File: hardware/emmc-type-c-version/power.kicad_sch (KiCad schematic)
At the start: 25 parts, among them SW301 RESET SW, U301 SPX3819M5-L

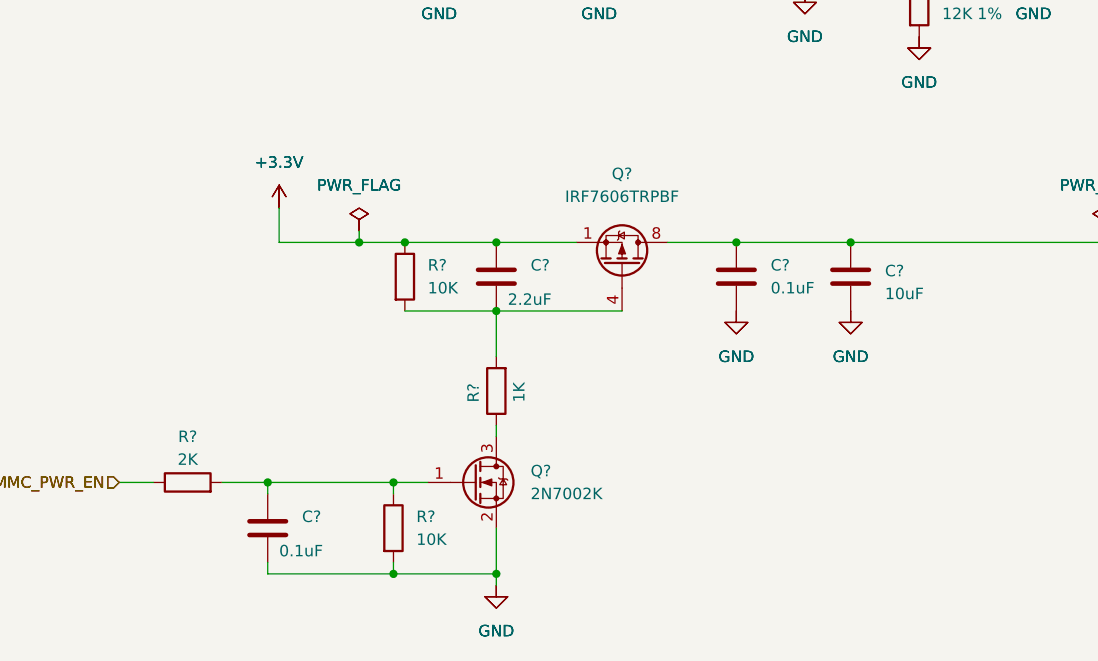
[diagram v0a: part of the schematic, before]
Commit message: Corrected part number in the BOM
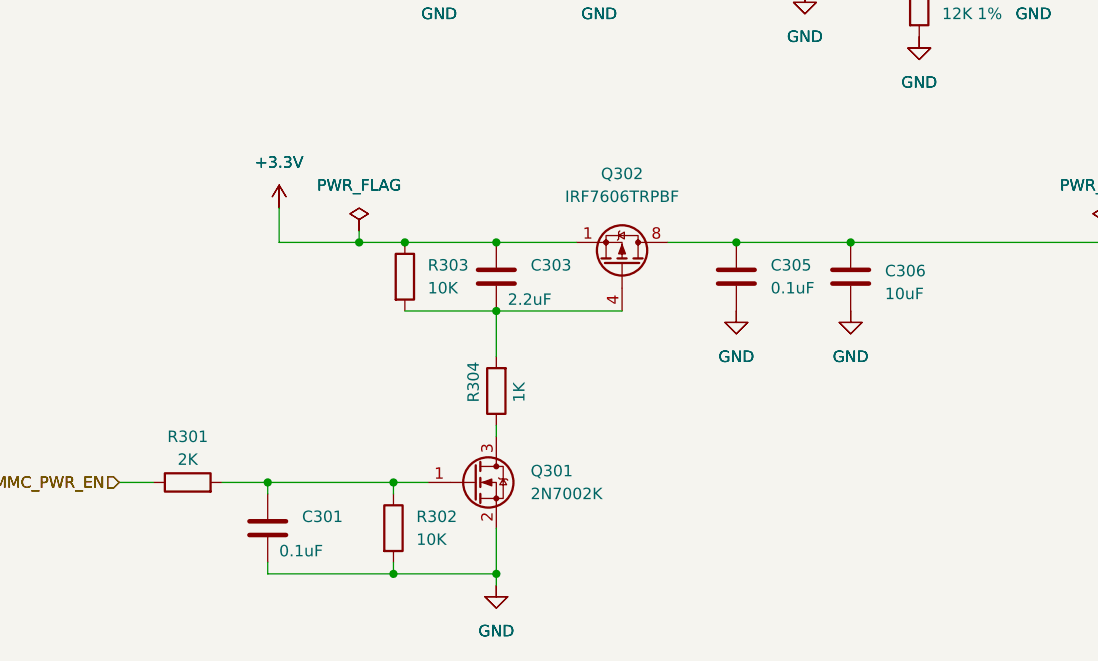
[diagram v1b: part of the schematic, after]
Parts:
- C304, C308: digikey 311-3494-1-ND -> 311-1355-1-ND; storeURL https://www.digikey.com/en/products/detail/yageo/CC0603MRX5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 -> https://www.digikey.com/en/products/detail/yageo/CC0805ZKY5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
- C306: renamed from C?; digikey 311-3494-1-ND -> 311-1355-1-ND; storeURL https://www.digikey.com/en/products/detail/yageo/CC0603MRX5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 -> https://www.digikey.com/en/products/detail/yageo/CC0805ZKY5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
- FB301: footprint tbctl:L_0603_1608Metric_Pad1.05x0.95mm_HandSolder -> Inductor_SMD:L_0603_1608Metric_Pad1.05x0.95mm_HandSolder; digikey 240-2399-1-ND -> 490-1014-1-ND; storeURL https://www.digikey.com/en/products/detail/laird-signal-int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 -> https://www.digikey.com/en/products/detail/murata-electroni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
- R301: renamed from R?; footprint tbctl:R_0805_2012Metric_Pad1.20x1.40mm_HandSolder -> Resistor_SMD:R_0805_2012Metric_Pad1.20x1.40mm_HandSolder; digikey 311-2.0KGRCT-ND -> 311-2.0KARCT-ND; storeURL https://www.digikey.com/en/products/detail/yageo/RC0603JR-0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 -> https://www.digikey.com/en/products/detail/yageo/RC0805JR-0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
- R302, R303: renamed from R?; footprint tbctl:R_0805_2012Metric_Pad1.20x1.40mm_HandSolder -> Resistor_SMD:R_0805_2012Metric_Pad1.20x1.40mm_HandSolder; digikey 13-RC0603JR-1010KLCT-ND -> 311-10KARCT-ND; storeURL https://www.digikey.com/en/products/detail/yageo/RC0603JR-1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 -> https://www.digikey.com/en/products/detail/yageo/RC0805JR-0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
- R304: renamed from R?; footprint tbctl:R_0805_2012Metric_Pad1.20x1.40mm_HandSolder -> Resistor_SMD:R_0805_2012Metric_Pad1.20x1.40mm_HandSolder; digikey 13-RC0603JR-101KLCT-ND -> 311-1.0KARCT-ND; storeURL https://www.digikey.com/en/products/detail/yageo/RC0603JR-1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 -> https://www.digikey.com/en/products/detail/yageo/RC0805JR-0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
- R305: footprint tbctl:R_0805_2012Metric_Pad1.20x1.40mm_HandSolder -> Resistor_SMD:R_0805_2012Metric_Pad1.20x1.40mm_HandSolder; digikey 13-RC0603FR-1320KLCT-ND -> 311-20.0KCRCT-ND; storeURL https://www.digikey.com/en/products/detail/yageo/RC0603FR-1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 -> https://www.digikey.com/en/products/detail/yageo/RC0805FR-0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
- R306: footprint tbctl:R_0805_2012Metric_Pad1.20x1.40mm_HandSolder -> Resistor_SMD:R_0805_2012Metric_Pad1.20x1.40mm_HandSolder; digikey 311-12.0KHRCT-ND -> 311-12.0KCRCT-ND; storeURL https://www.digikey.com/en/products/detail/yageo/RC0603FR-0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 -> https://www.digikey.com/en/products/detail/yageo/RC0805FR-0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
- R307, R309: footprint tbctl:R_0805_2012Metric_Pad1.20x1.40mm_HandSolder -> Resistor_SMD:R_0805_2012Metric_Pad1.20x1.40mm_HandSolder; digikey 13-RC0603JR-101KLCT-ND -> 311-1.0KARCT-ND; storeURL https://www.digikey.com/en/products/detail/yageo/RC0603JR-1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 -> https://www.digikey.com/en/products/detail/yageo/RC0805JR-0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
- R308: footprint tbctl:R_0805_2012Metric_Pad1.20x1.40mm_HandSolder -> Resistor_SMD:R_0805_2012Metric_Pad1.20x1.40mm_HandSolder; digikey 13-RC0603JR-1010KLCT-ND -> 311-10KARCT-ND; storeURL https://www.digikey.com/en/products/detail/yageo/RC0603JR-1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 -> https://www.digikey.com/en/products/detail/yageo/RC0805JR-0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
- gave numbers to parts that had none: 5
